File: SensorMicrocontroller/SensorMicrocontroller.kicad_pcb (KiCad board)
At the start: 2 copper layers, 100 x 100 mm, 41 parts, among them J1 JST B4B-PH-SM4-TB, J2 JST B4B-PH-SM4-TB, J3 JST B6B-PH-SM4-TB, J4 JST B4B-PH-SM4-TB, J5 JST B4B-PH-SM4-TB, J8 12V Connector, J9 Light Connector, Q1 DMT6009LCT, Q2 DMT6009LCT, U1 ADS1115IDGS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

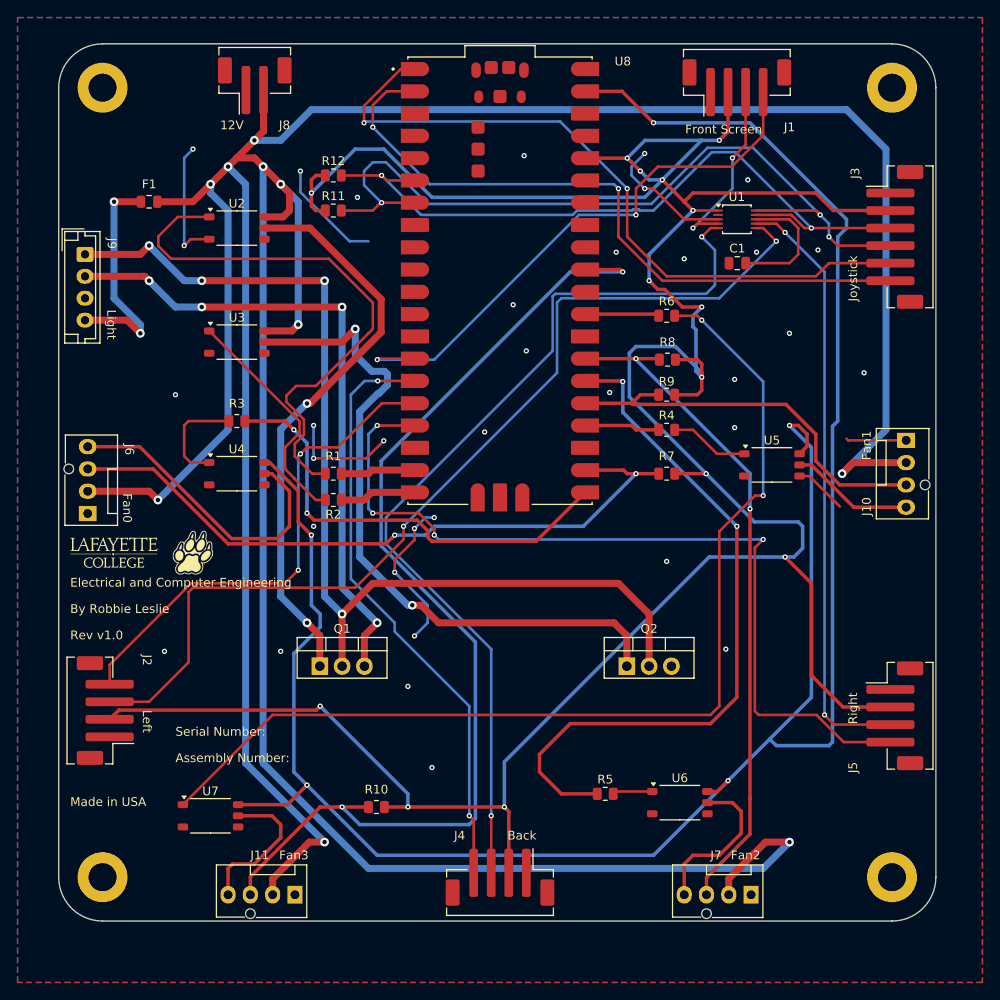
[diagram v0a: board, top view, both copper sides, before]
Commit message: Added caps for photocouplers
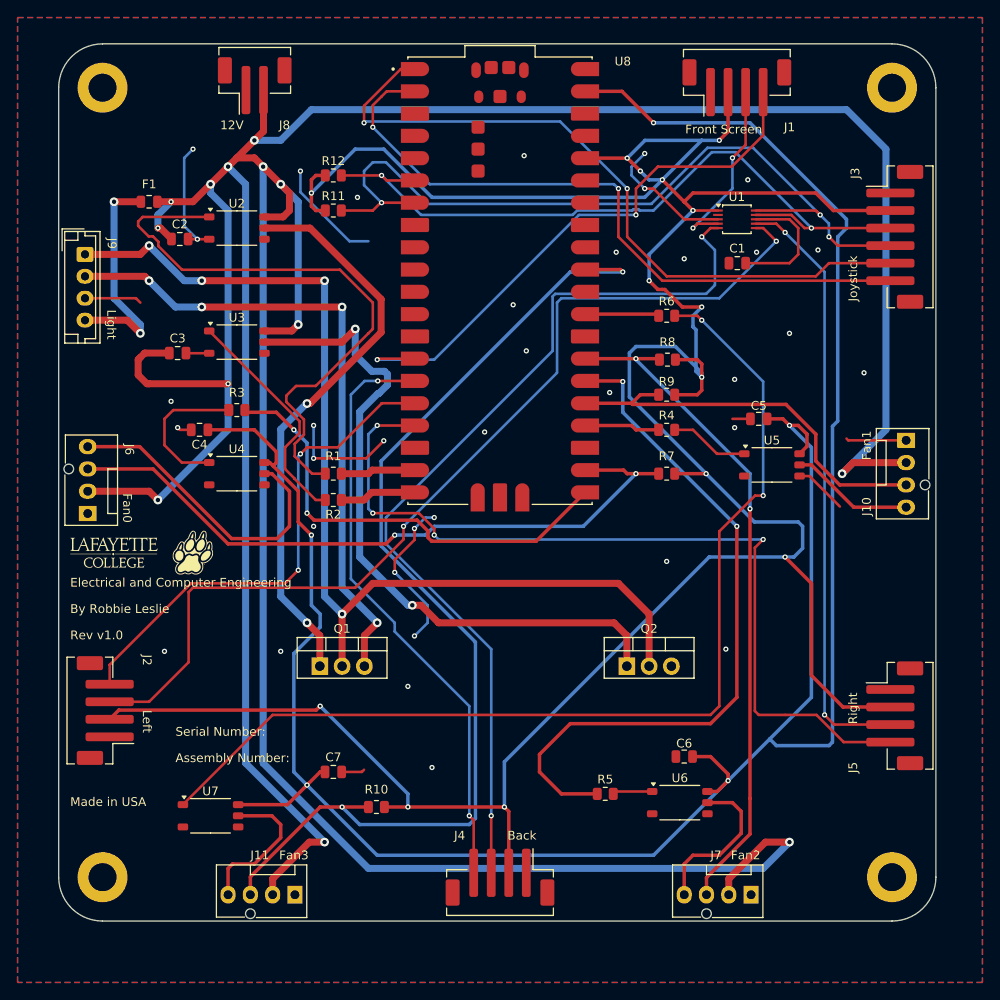
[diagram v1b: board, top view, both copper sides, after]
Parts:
- added C2: 0.1uF, Capacitor_SMD:C_0805_2012Metric, F.Cu at (108.5, 70.2)
- added C3: 0.1uF, Capacitor_SMD:C_0805_2012Metric, F.Cu at (108.2, 83.2)
- added C4: 0.1uF, Capacitor_SMD:C_0805_2012Metric, F.Cu at (110.8, 92.0)
- added C5: 0.1uF, Capacitor_SMD:C_0805_2012Metric, F.Cu at (174.5, 90.8)
- added C6: 0.1uF, Capacitor_SMD:C_0805_2012Metric, F.Cu at (166.0, 129.2)
- added C7: 0.1uF, Capacitor_SMD:C_0805_2012Metric, F.Cu at (126.0, 131.0)
- moved R3 1.25 mm to (115.0, 89.8)
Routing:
- net /12V: track 460.4 -> 482.3 mm, vias 10 -> 13
- net /5V: track 262.3 -> 284.1 mm
- net /GND: track 85.7 -> 100.4 mm, vias 35 -> 36
- net Net-(U4-Anode): track 11.9 -> 16.7 mm
- net Net-(U2-Anode): track 63.4 -> 68.0 mm
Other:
- board text added: "2/3/25"
- board text removed: "2/2/25"

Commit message: Updated fill
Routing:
- net /GND: vias 36 -> 39
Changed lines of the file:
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@@
+	)
+	(via
+		(at 170.75 96.25)
+		(size 0.6)
+		(drill 0.3)
+		(layers "F.Cu" "B.Cu")
+		(free yes)
+		(net 2)
 	)
 	(via
@@
 	)
 	(via
+		(at 180 126.5)
+		(size 0.6)
+		(drill 0.3)
+		(layers "F.Cu" "B.Cu")
+		(free yes)
+		(net 2)
+	)
+	(via
 		(at 158.25 71.75)
 		(size 0.6)
@@
 		(size 0.6)
 		(drill 0.3)
+		(layers "F.Cu" "B.Cu")
+		(free yes)
+		(net 2)
+	)
+	(via
+		(at 175.5 62.75)
+		(size 0.6)
+		(drill 0.3)

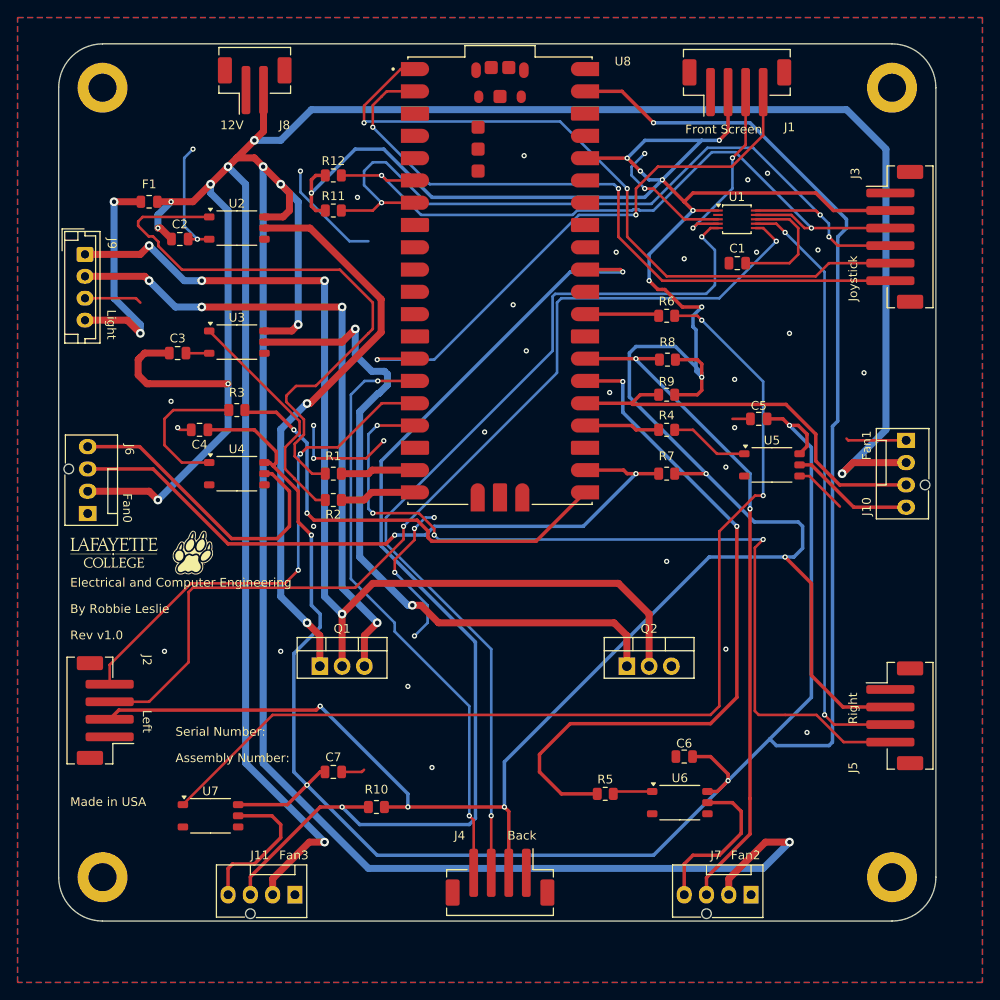
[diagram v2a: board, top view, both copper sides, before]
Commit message: Updated routing
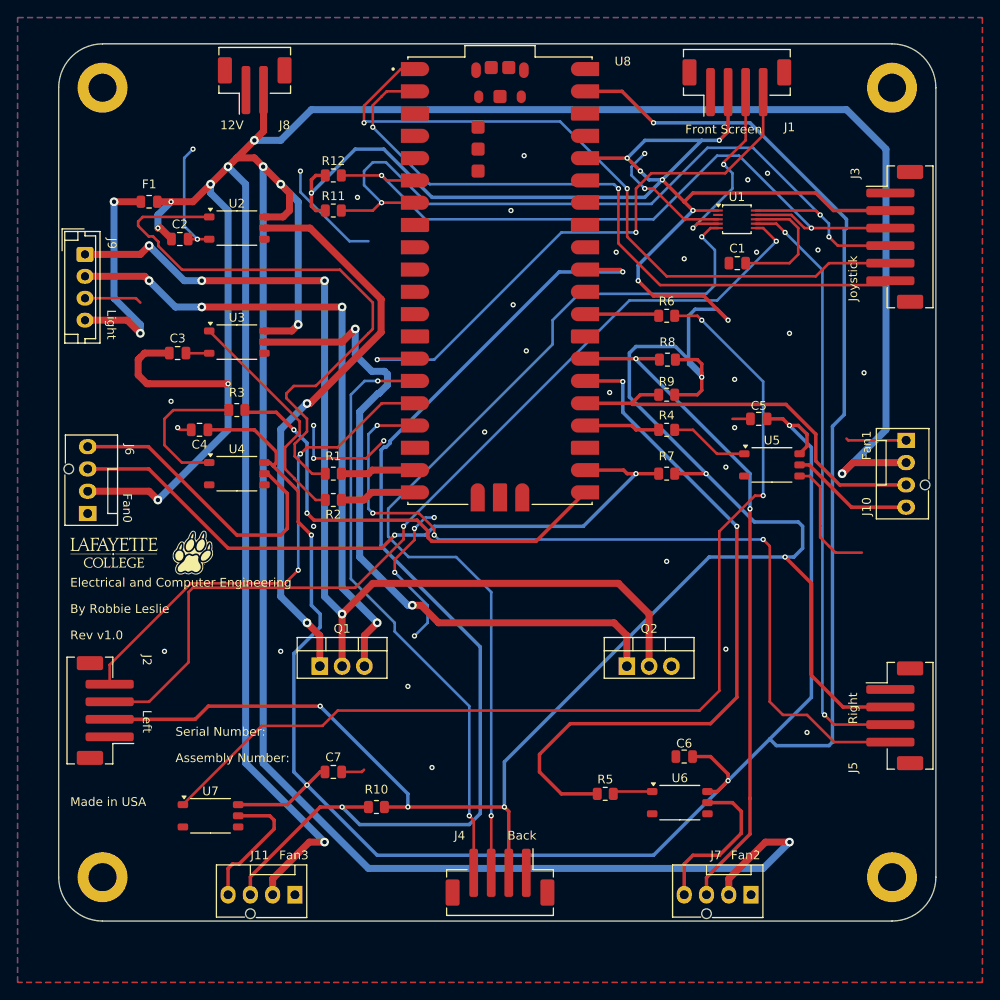
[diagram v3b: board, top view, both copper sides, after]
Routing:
- net /3.3V: track 336.8 -> 346.3 mm
- net /GND: track 100.4 -> 108.4 mm, vias 39 -> 40
- net /US2: track 111.0 -> 106.3 mm
- net /PIR3: track 98.0 -> 95.6 mm
- net /PWM3 5V: track 17.2 -> 15.4 mm
- net /US1: track 106.0 -> 107.4 mm
- net /Fan Sense3: track 121.2 -> 122.5 mm
- net /PIR0: track 65.6 -> 66.8 mm
- net Net-(U7-Anode): track 118.6 -> 117.6 mm
- net /TXFinger: track 77.4 -> 78.3 mm
- net /PWM0 5V: track 35.6 -> 34.8 mm
- net /US0: track 21.0 -> 21.9 mm

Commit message: Removed fan optoisolators after testing them
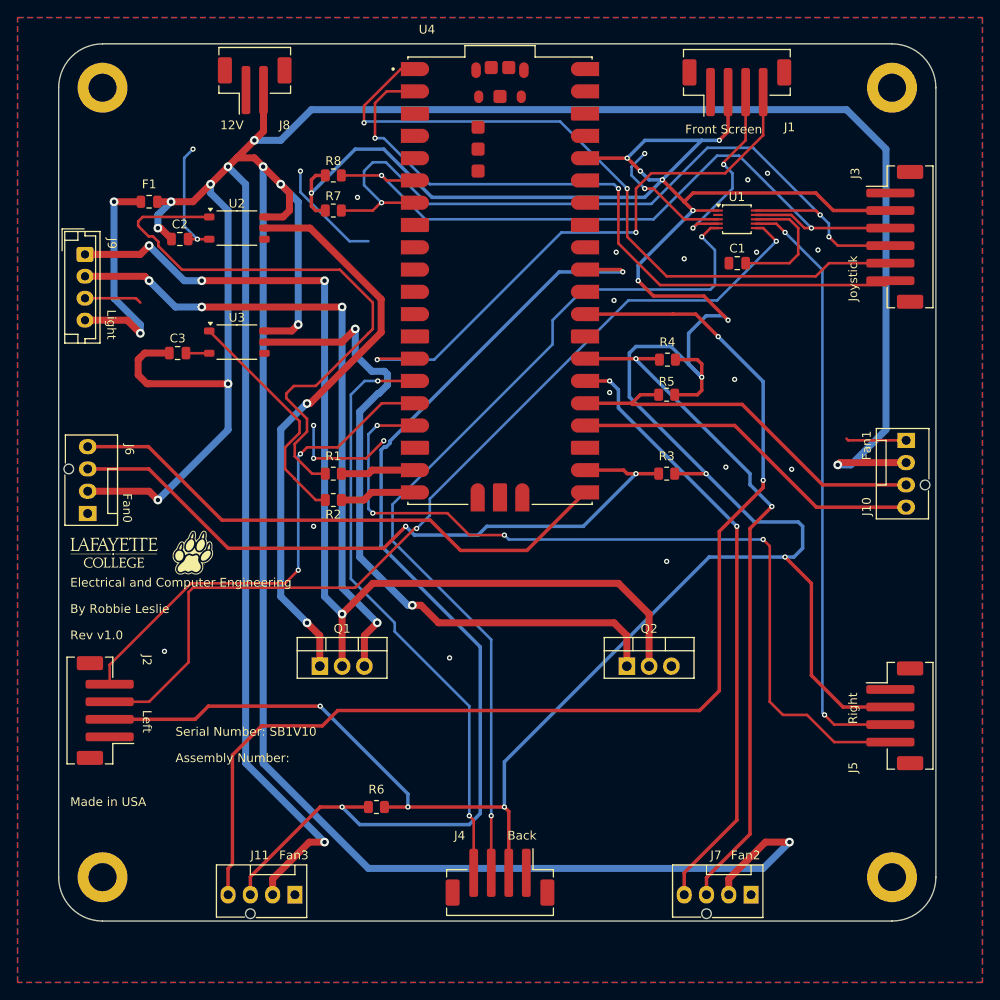
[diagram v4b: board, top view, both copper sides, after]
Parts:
- removed C4, C5, C6, C7: 0.1uF, Capacitor_SMD:C_0805_2012Metric
- removed the G*** at (110.0, 106.0)
- removed the R3 at (115.0, 89.8)
- removed the R4 at (164.0, 92.0)
- removed the R5 at (157.0, 133.5)
- removed the R6 at (164.0, 79.0)
- removed the U4 at (115.0, 97.0)
- removed U5, U6, U7: Optoisolators, Package_SO:SO-5-6_4.55x3.7mm_P1.27mm
- added G***: LOGO, CustomFootprints:LeopardPawFootprint, F.Cu at (110.0, 106.0)
- U4: renamed from U8; footprint Footprints:pico -> CustomFootprints:pico
- renumbered R7 to R3, R8 to R4, R9 to R5, R10 to R6, R11 to R7, R12 to R8
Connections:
- J10 pad 4: /PWM1 5V -> /PWM1
- J11 pad 4: /PWM3 5V -> /PWM3
- J6 pad 4: /PWM0 5V -> /PWM0
- J7 pad 4: /PWM2 5V -> /PWM2
- U4 pad 21: /PWM0 3.3V -> /PWM0
- U4 pad 24: /PWM1 3.3V -> /PWM1
- U4 pad 26: /PWM2 3.3V -> /PWM2
- U4 pad 29: /PWM3 3.3V -> /PWM3
- U4 pad 39: /5V -> unconnected-(U4-VSYS-Pad39)
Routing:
- net /5V: track 284.1 -> 0.00 mm, vias 5 -> 0
- net /PWM3: track 0.00 -> 135.5 mm, vias 0 -> 2
- net Net-(U7-Anode): track 117.6 -> 0.00 mm, vias 2 -> 0
- net /PWM2 3.3V: track 80.5 -> 0.00 mm, vias 2 -> 0
- net /PWM2: track 0.00 -> 69.9 mm, vias 0 -> 2
- net /PWM0: track 0.00 -> 64.3 mm
- net /PWM0 3.3V: track 52.3 -> 0.00 mm, vias 2 -> 0
- net /PWM1: track 0.00 -> 40.5 mm
- net /GND: track 108.4 -> 69.9 mm, vias 40 -> 24
- net /PWM0 5V: track 34.8 -> 0.00 mm
- net /PWM2 5V: track 18.2 -> 0.00 mm
- net Net-(U4-Anode): track 16.7 -> 0.00 mm
- net /PWM3 5V: track 15.4 -> 0.00 mm
- net /PWM1 5V: track 14.1 -> 0.00 mm
- net Net-(U5-Anode): track 9.07 -> 0.00 mm
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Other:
- board text added: "Board Part Number: 1"
- board text added: "Serial Number: SB1V10"
- board text added: "Serial number SB1V10 stands for {dblquote}Sensor Board Design 1 v1.0{dblquote}"
- board text removed: "1.0"
- board text removed: "2/3/25"
- board text removed: "Board Part Number:"
- board text removed: "Sensor Microcontroller PCB"
- board text removed: "Serial Number:"

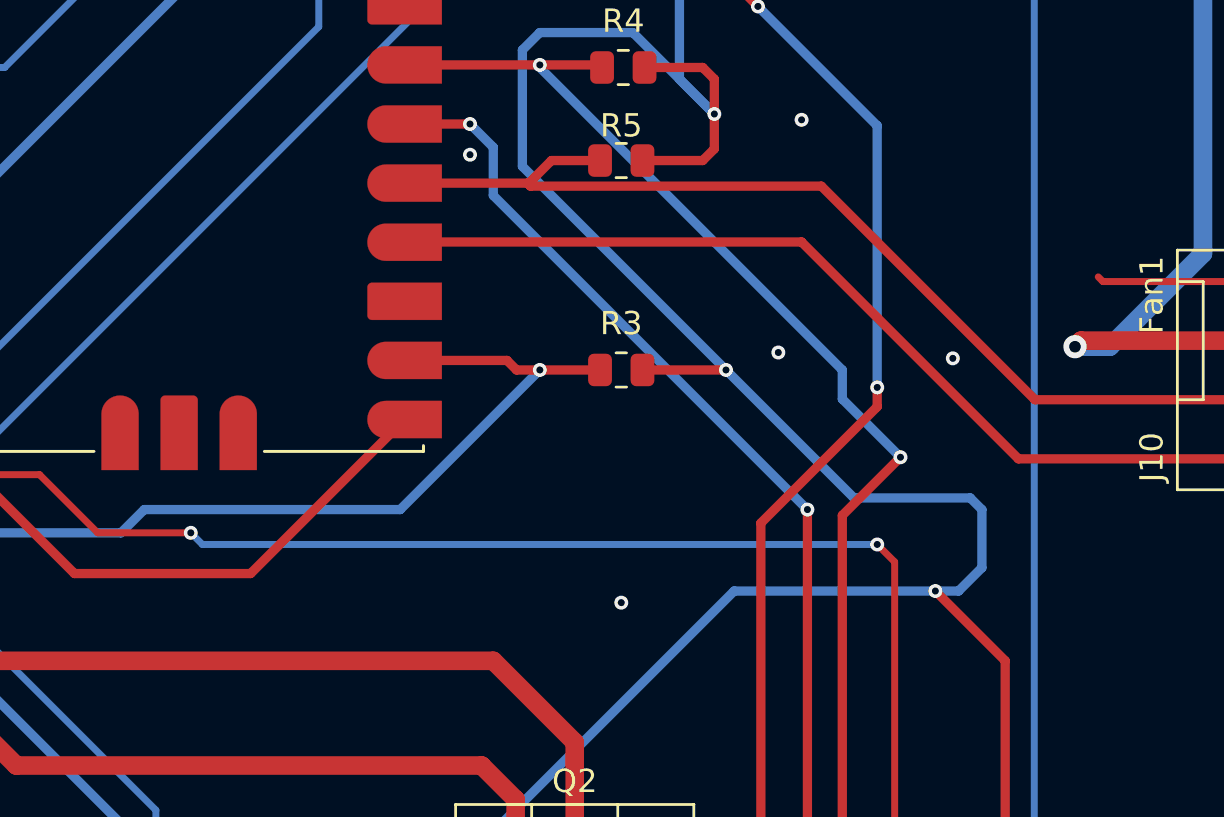
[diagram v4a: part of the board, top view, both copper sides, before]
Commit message: Added pull up for light transistor after testing
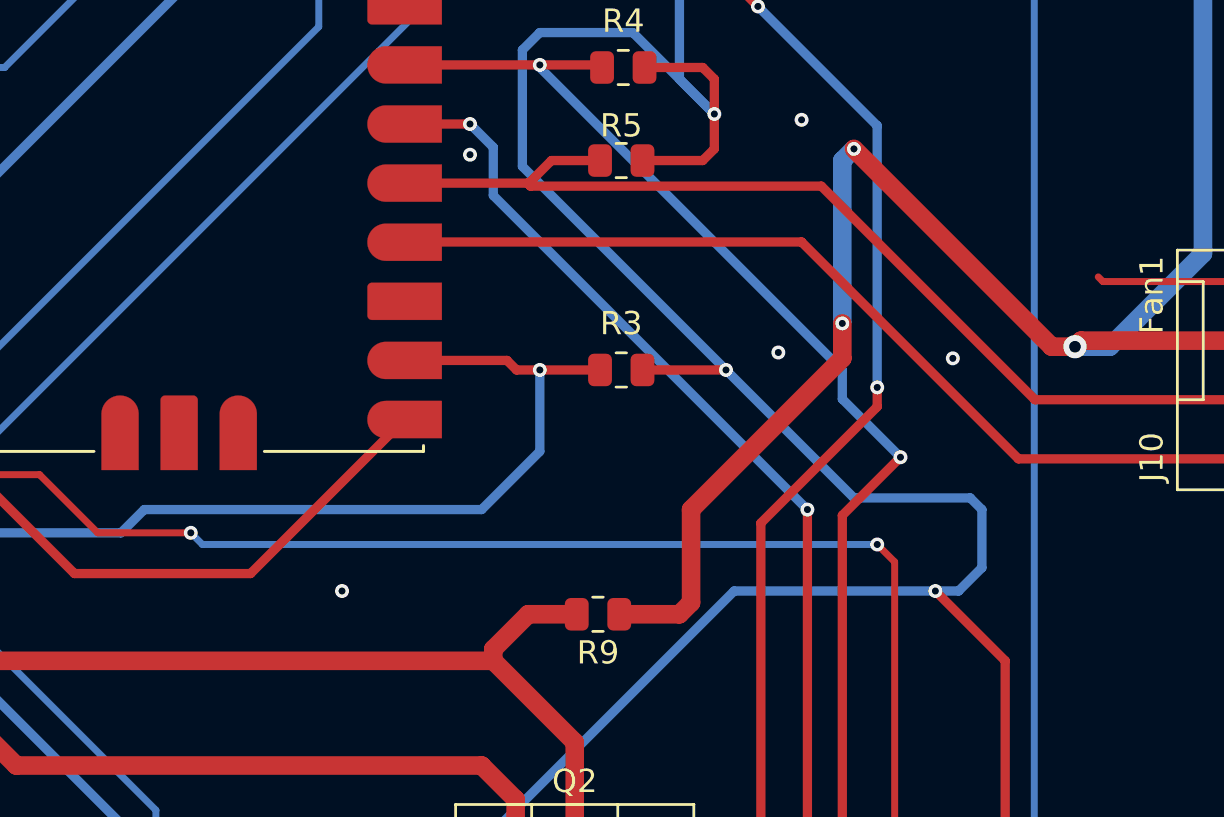
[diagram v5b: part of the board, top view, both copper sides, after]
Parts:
- added R9: 10k, Resistor_SMD:R_0805_2012Metric, F.Cu at (163.0, 107.5)
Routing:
- net /12V: track 482.5 -> 521.2 mm, vias 13 -> 15
- net /Light Red Wire: track 118.0 -> 122.7 mm
- net /Fan Sense0: track 79.2 -> 81.2 mm

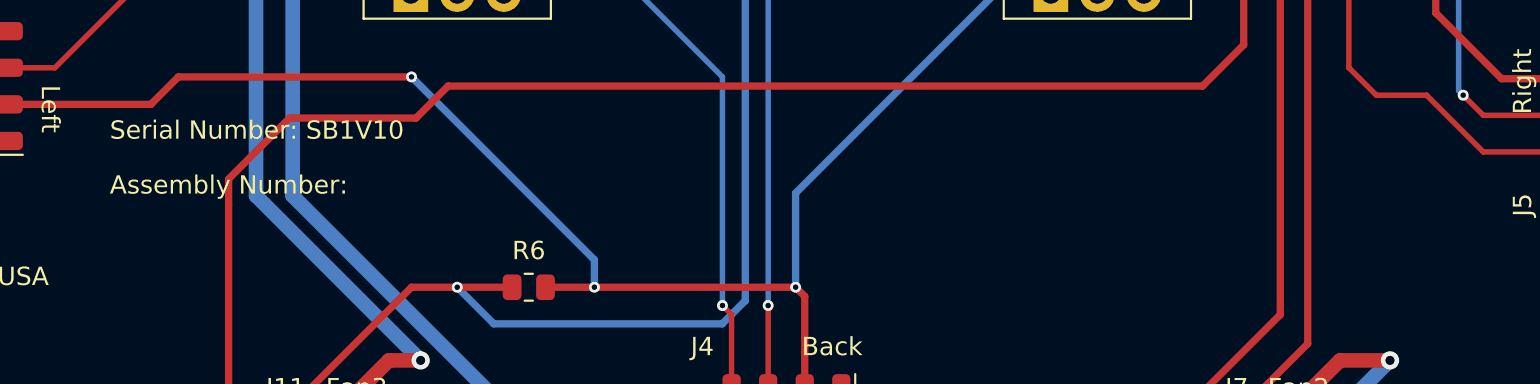
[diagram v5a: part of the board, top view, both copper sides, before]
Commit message: Updated silkscreen
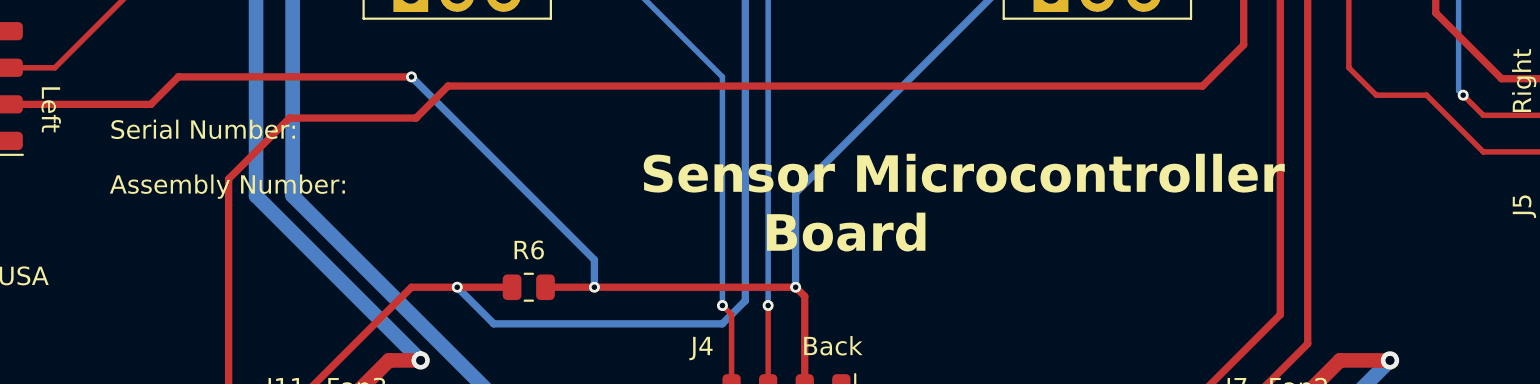
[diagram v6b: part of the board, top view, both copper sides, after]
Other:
- board text added: "Sensor Microcontroller Board"
- board text added: "Serial Number:"
- board text removed: "Serial Number: SB1V10"
- board text removed: "Serial number SB1V10 stands for {dblquote}Sensor Board Design 1 v1.0{dblquote}"
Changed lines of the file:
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@@
 		(tags "resistor")
 		(property "Reference" "R9"
-			(at 0 -1.65 360)
+			(at 0 -1.65 0)
 			(layer "F.SilkS")
 			(effects
@@
 		)
 		(property "Value" "10k"
-			(at 0 1.65 360)
+			(at 0 1.65 0)
 			(layer "F.Fab")
 			(effects
@@
 		)
 		(fp_text user "${REFERENCE}"
-			(at 0 0 360)
+			(at 0 0 0)
 			(layer "F.Fab")
 			(effects
@@
 		)
 	)
-	(gr_text "Serial Number: SB1V10"
+	(gr_text "Sensor Microcontroller\n	   Board"
+		(at 137 133.25 0)
+		(layer "F.SilkS")
+		(effects
+			(font
+				(size 2 2)
+				(thickness 0.3)
+				(bold yes)
+			)
+			(justify left bottom)
+		)
+	)
+	(gr_text "Serial Number:"
 		(at 108 127 0)
 		(layer "F.SilkS")
@@
 			)
 			(justify left bottom)
-		)
-	)
-	(gr_text "Serial number SB1V10\nstands for {dblquote}Sensor Board Design 1 v1.0{dblquote}"
-		(at 122.25 131.75 0)
-		(layer "Cmts.User")
-		(effects
-			(font
-				(size 1.5 1.5)
-				(thickness 0.3)
-				(bold yes)
-			)
-			(justify left bottom)
